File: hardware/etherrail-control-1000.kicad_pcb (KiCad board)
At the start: 2 copper layers, 15.9 x 27.9 mm, 33 parts, among them J1 Conn_02x04_Odd_Even, J2 Conn_01x04, U1 AMS1117-3.3, U2 ESP32-C3, Y2 Crystal_GND24

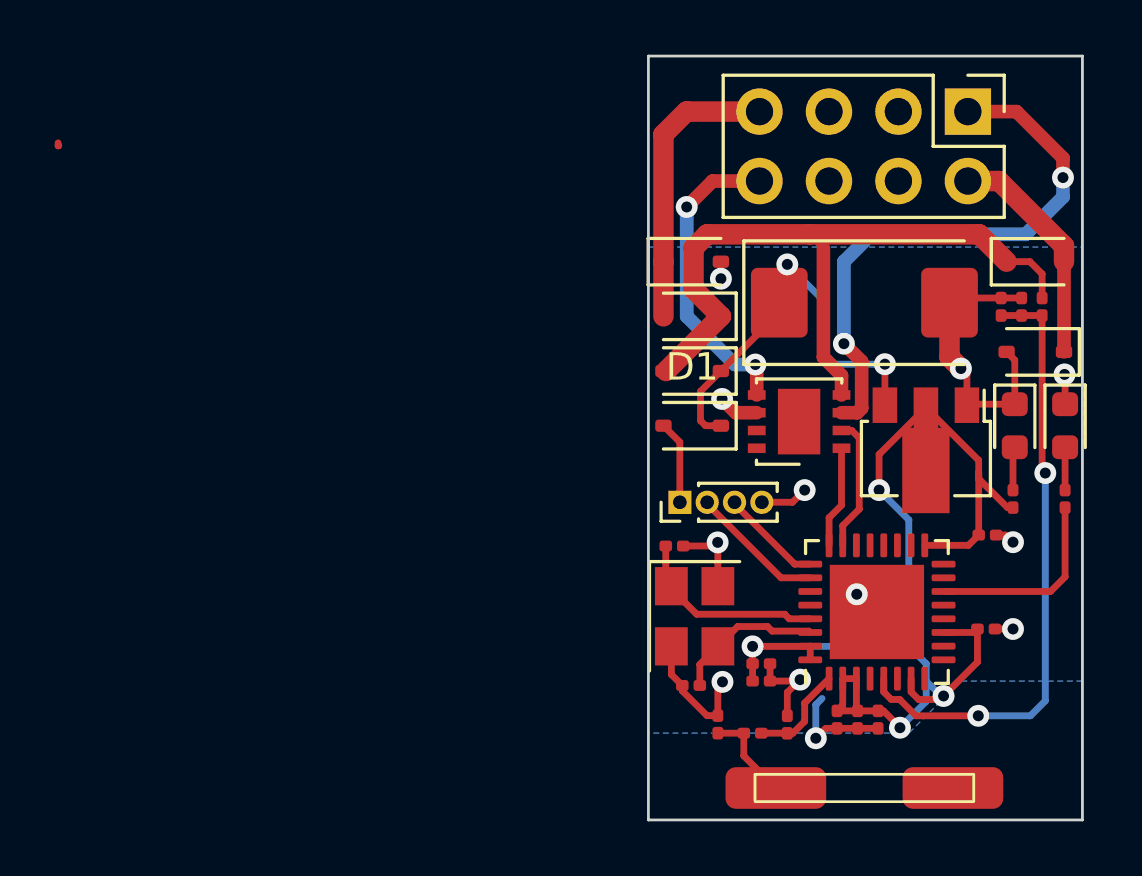
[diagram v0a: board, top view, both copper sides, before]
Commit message: Add 0402 10uF filter cap to board
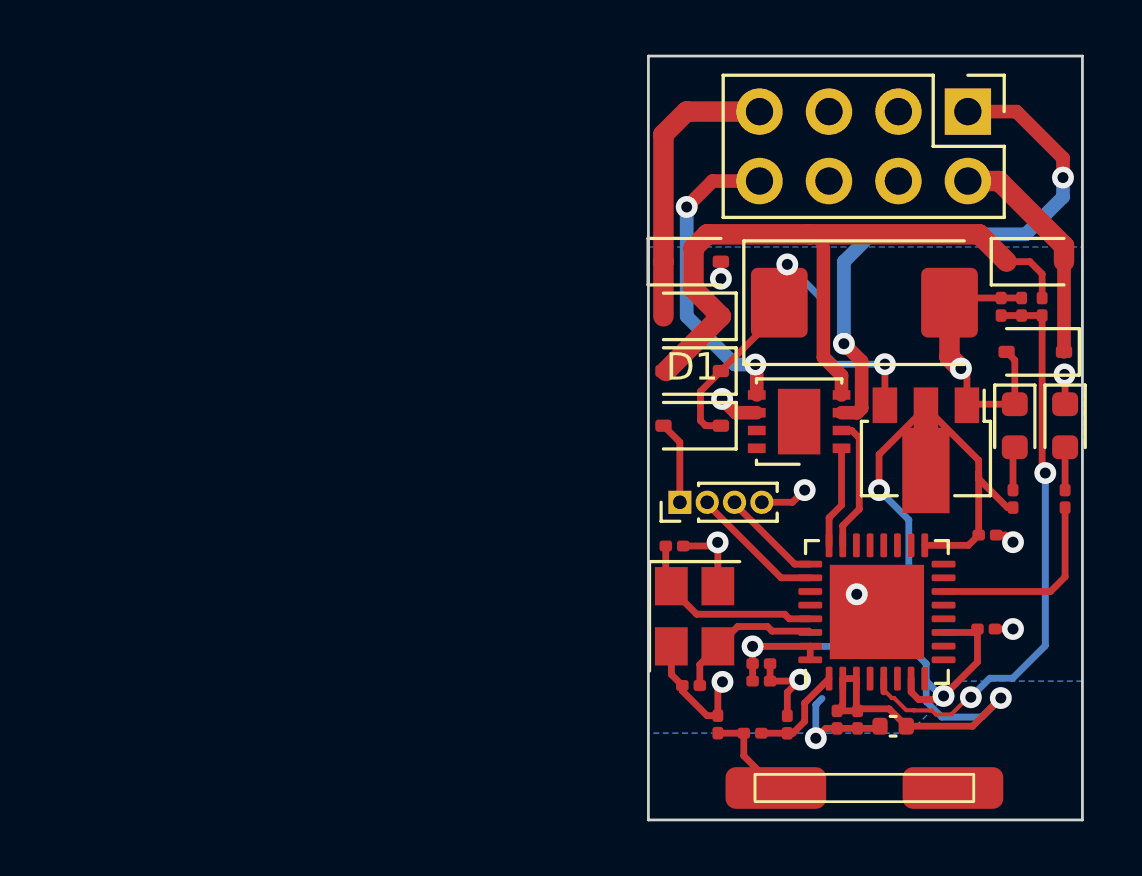
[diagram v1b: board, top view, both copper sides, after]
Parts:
- C4: footprint Capacitor_SMD:C_0201_0603Metric -> Capacitor_SMD:C_0402_1005Metric
- moved C4 0.60 mm to (110.5, 55.0), turned to 180 degrees
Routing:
- net /Controller Power: track 45.8 -> 51.8 mm
- net /Power Sensing Input: track 22.6 -> 21.5 mm
